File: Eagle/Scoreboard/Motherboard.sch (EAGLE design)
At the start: 30 parts

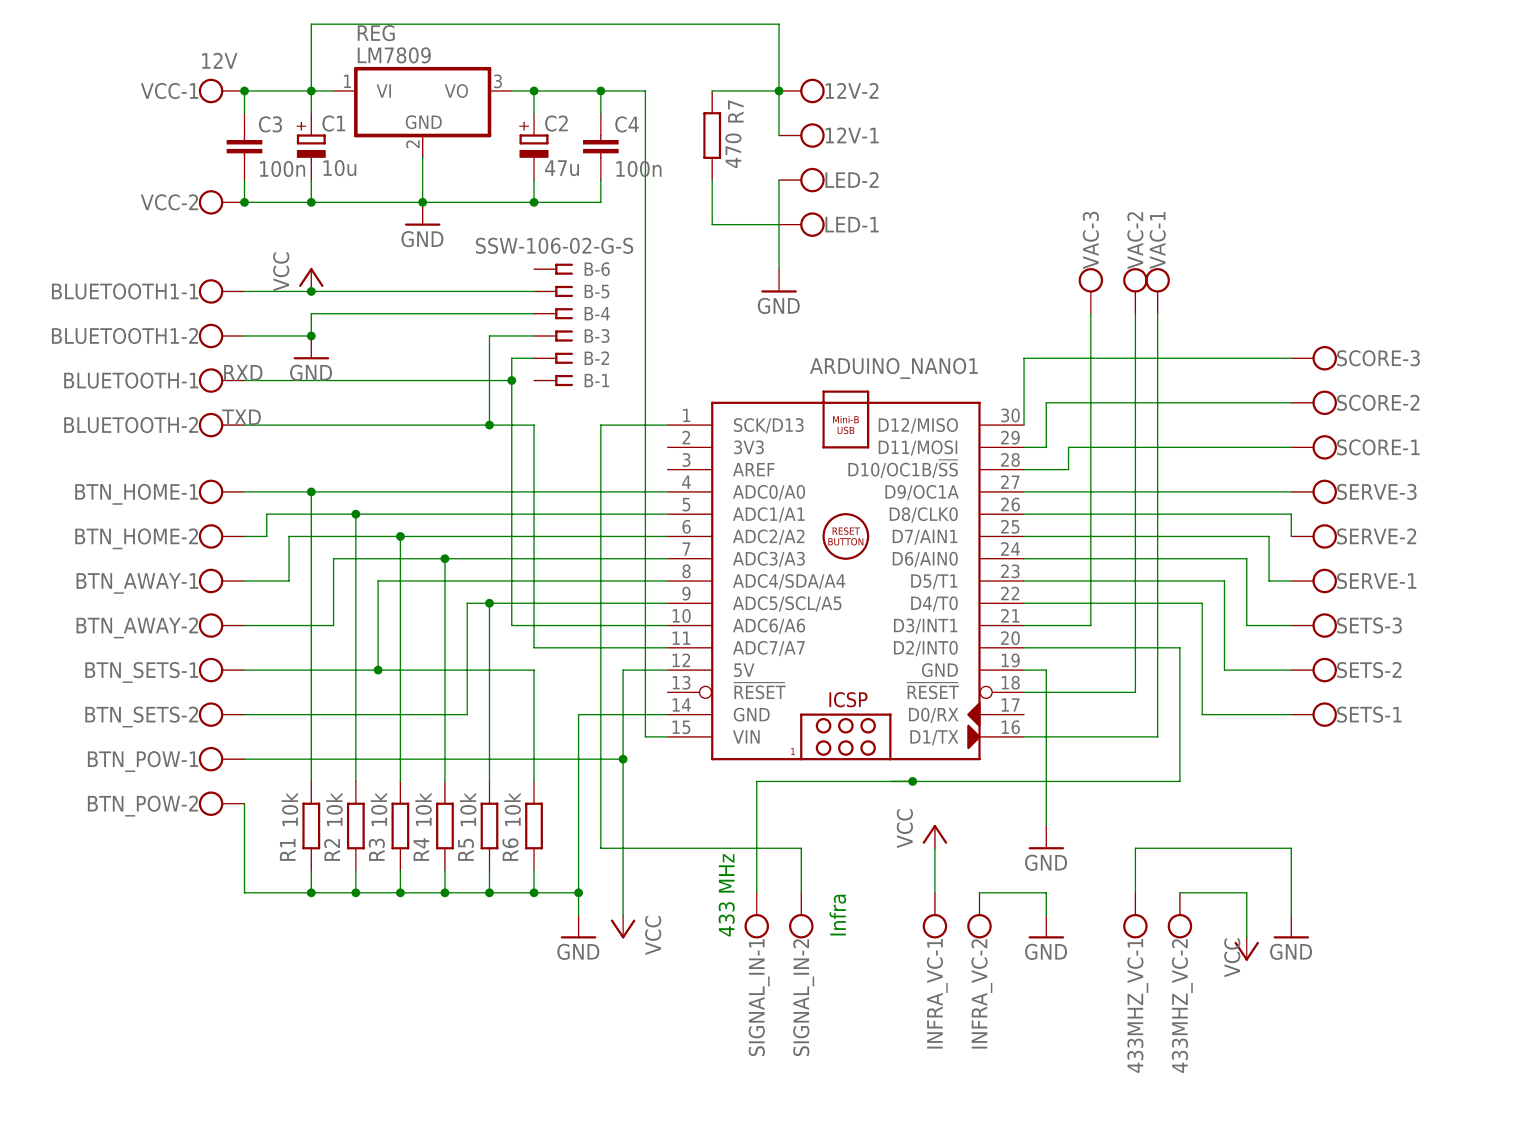
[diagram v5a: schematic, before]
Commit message: Fixed error with A6, A7 pin plus couple major changes
The pin A6 & A7 cannot be used for anything digital on Nano. So removed
Also moved the bluetooth pins and removed buttons for sets to get some free pin.  Made the bluetooth module powered by 3.3V so we don't need to use voltage divider. Also made the 9V available so we can use it for powering all the score controllers
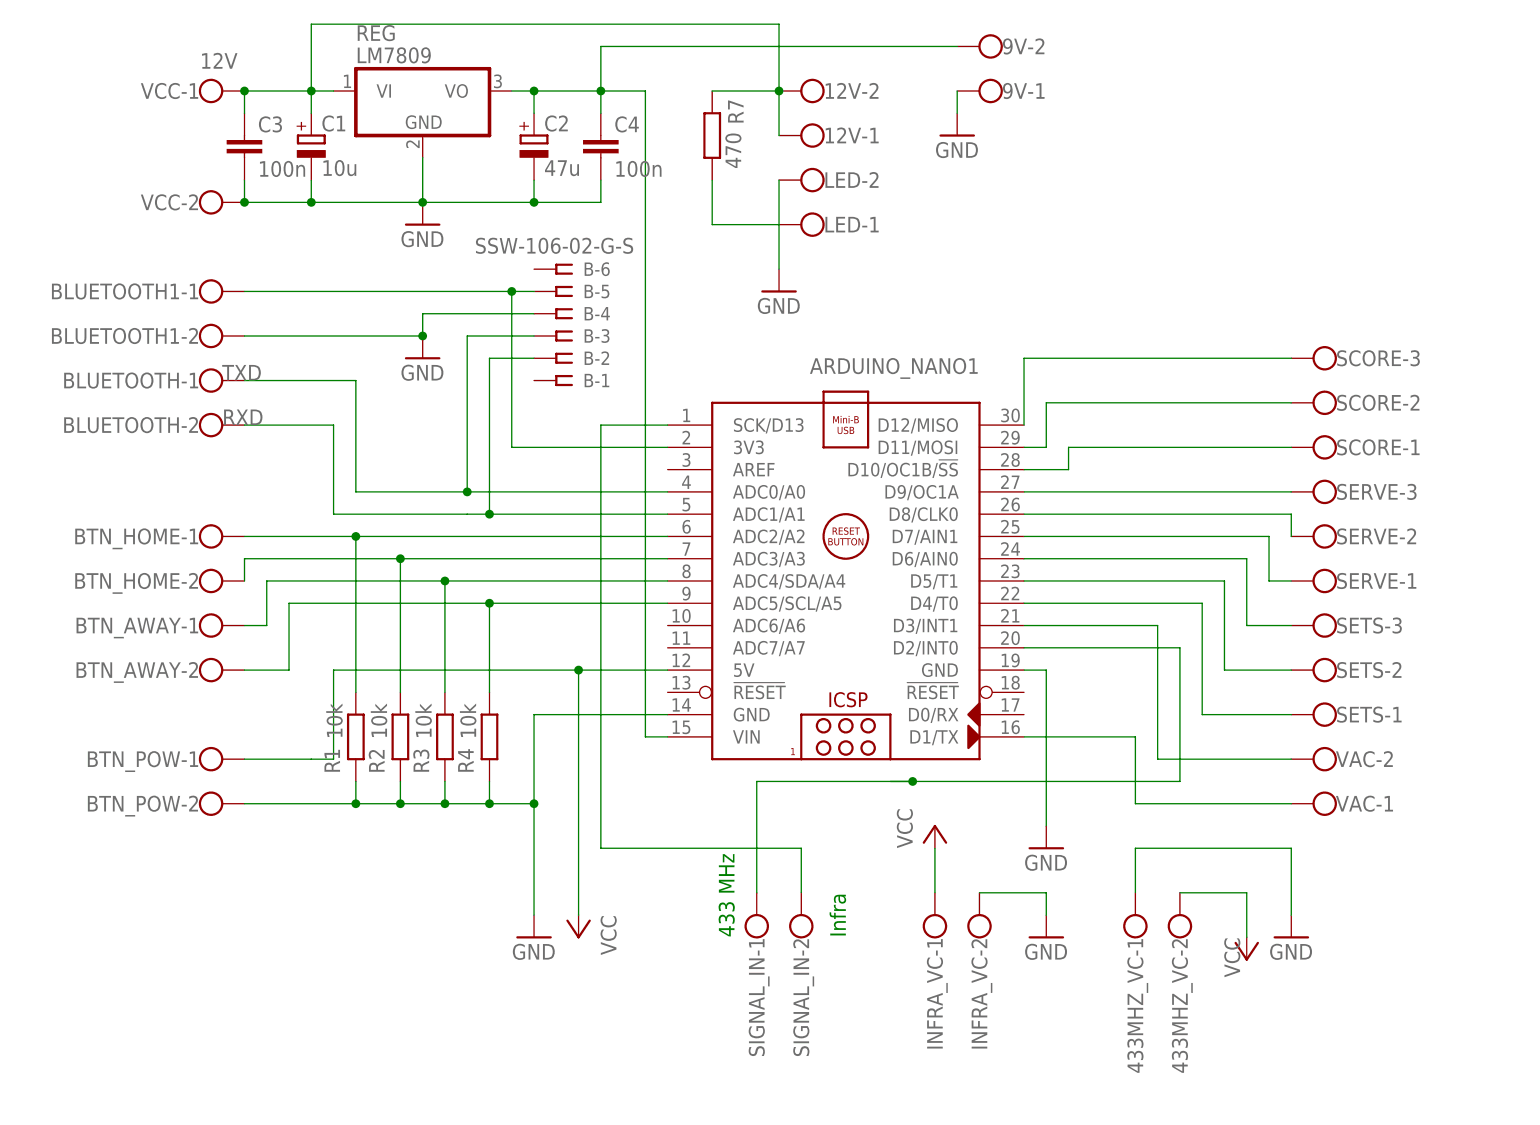
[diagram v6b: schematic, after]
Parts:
- removed BTN_SETS: (no value), con-wago-500:W237-102
- removed R5, R6: 10k, resistor:R-EU_0204/7
- added 9V: (no value), con-wago-500:W237-102
- VAC: device con-wago-500:W237-103 -> con-wago-500:W237-102
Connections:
- net VAC1 renamed N$6
- removed net N$6 (its old number): ARDUINO_NANO1.ADC5/SCL/A5, BTN_SETS-2.KL, R5.1
- removed net RESET: ARDUINO_NANO1.!RESET@1, VAC-2.KL
- removed net VAC3: ARDUINO_NANO1.D3/INT1, VAC-3.KL
- new net 3V3: ARDUINO_NANO1.3V3, B-5.1, BLUETOOTH1-1.KL
- net GND: now also 9V-1.KL; no longer R5.2, R6.2
- net N$1: now also ARDUINO_NANO1.ADC2/A2; no longer ARDUINO_NANO1.ADC0/A0
- net N$2: now also ARDUINO_NANO1.ADC3/A3; no longer ARDUINO_NANO1.ADC1/A1
- net N$3: now also ARDUINO_NANO1.ADC4/SDA/A4; no longer ARDUINO_NANO1.ADC2/A2
- net N$4: now also ARDUINO_NANO1.ADC5/SCL/A5; no longer ARDUINO_NANO1.ADC3/A3
- net N$5: now also ARDUINO_NANO1.D3/INT1, VAC-2.KL; no longer ARDUINO_NANO1.ADC4/SDA/A4, BTN_SETS-1.KL, R6.1
- net RXD: now also ARDUINO_NANO1.ADC1/A1, BLUETOOTH-2.KL; no longer ARDUINO_NANO1.ADC6/A6, BLUETOOTH-1.KL
- net TXD: now also ARDUINO_NANO1.ADC0/A0, BLUETOOTH-1.KL; no longer ARDUINO_NANO1.ADC7/A7, BLUETOOTH-2.KL
- net VCC: no longer B-5.1, BLUETOOTH1-1.KL
- net VIN_9V: now also 9V-2.KL
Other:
- moved on the sheet: BTN_AWAY-1, BTN_AWAY-2, BTN_HOME-1, BTN_HOME-2, R1, R2, R3, R4, VAC-1, VAC-2

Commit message: Added code for turning the scoreboard to clock mode
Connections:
- net N$3 renamed A4
- net N$4 renamed A5
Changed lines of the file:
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@@
 </segment>
 </net>
-<net name="N$3" class="0">
+<net name="A4" class="0">
 <segment>
 <pinref part="ARDUINO_NANO1" gate="G$1" pin="ADC4/SDA/A4"/>
@@
 </segment>
 </net>
-<net name="N$4" class="0">
+<net name="A5" class="0">
 <segment>
 <pinref part="ARDUINO_NANO1" gate="G$1" pin="ADC5/SCL/A5"/>
